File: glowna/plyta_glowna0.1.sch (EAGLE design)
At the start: 111 parts, among them IC1 4504D, Q1 CSM-7X-DU, Q2 N-HEXFET-2D_SOT232-IRLL014N, Q3 N-HEXFET-2D_SOT232-IRLL014N, Q4 N-HEXFET-2D_SOT232-IRLL014N, Q5 N-HEXFET-2D_SOT232-IRLL014N, Q6 N-HEXFET-2D_SOT232-IRLL014N, X1 MINI-USB_SHIELD5P2-32005-601

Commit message: indukcyjne
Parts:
- removed JP23: (no value), pinhead:PINHD-1X2
- added D8: BAT54S, diode:BAT54S
- added JP27: (no value), pinhead:PINHD-1X3
- C27: value 1uF -> 50nF
- R11: value 4,7k -> 5k
- R13: value 1k -> 15k
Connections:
- removed net N$16: JP23.2, R12.1
- new net N$38: JP27.1, R13.2
- net +12V: now also JP27.3; no longer R11.1
- net +3V3: now also D8.C2
- net ADC3_CZUJNIK_INDUKCYJNY: now also D8.C1A2, R11.1; no longer R11.2, R12.2
- net GND: now also D8.A1, JP27.2, R11.2; no longer R13.2
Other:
- moved on the sheet: C27, R11, R12, R13

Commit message: level shifter
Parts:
- added D_1, D_2, D_3, D_4, D_5, D_6: (no value), diode:DIODE-DO-214AC
- added R16: 300, rcl:R-EU_R0603
- R12: value 330 -> 300
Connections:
- new net N$16: IC1P.VCC, R12.1
- new net N$39: IC1P.VDD, R16.1
- net +12V: now also D_5.C, D_6.C, R16.2; no longer IC1P.VCC
- net +24V: now also D_1.C, D_2.C, D_3.C, D_4.C
- net +3V3: now also R12.2
- net GND: no longer IC1P.VDD
- net N$11: now also D_6.A
- net N$12: now also D_1.A
- net N$15: now also D_5.A
- net N$17: now also D_3.A
- net N$18: now also D_4.A
- net N$20: now also D_2.A
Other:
- moved on the sheet: IC1P, R12

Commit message: rs i termistory
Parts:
- added C28, C29, C30: 1uF, rcl:C-EUC0603
- added D1, D2, D3, D4: BAT54S, diode:BAT54S
- added IC2: MAX481CSA, maxim:MAX481CSA
- added R17: 1k, rcl:R-EU_R0603
- added R18, R19, R20, R21: 10k, rcl:R-EU_R0603
- added U$19: TS9011SCX, v-reg:TS9011SCX
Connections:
- new net N$40: C28.2, IC2P.VCC, U$19.OUT
- new net N$42: C25.2, D3.C1A2, R19.2
- new net N$43: C24.2, D2.C1A2, R20.2
- new net N$44: C26.2, D4.C1A2, R18.2
- new net N$47: C23.2, D1.C1A2, R21.2
- net +12V: now also U$19.IN
- net +3V3: now also D1.C2, D2.C2, D3.C2, D4.C2
- net ADC_TER_1: now also R20.1; no longer C24.2
- net ADC_TER_2: now also R19.1; no longer C25.2
- net ADC_TER_3: now also R18.1; no longer C26.2
- net ADC_TER_BED: now also R21.1; no longer C23.2
- net GND: now also C28.1, C29.1, C30.1, D1.A1, D2.A1, D3.A1, D4.A1, IC2P.GND, U$19.GND
- net N$16: now also C29.2
- net N$39: now also C30.2
- net RS485_UART2_RTS: now also IC2G$1.DE, IC2G$1.RE/
- net RS485_UART2_TX: now also IC2G$1.DI, IC2G$1.RO, R17.1, R17.2

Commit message: kondensatory
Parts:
- added C31: 100uF, rcl:CPOL-EUUD-8X10
- added C32: 100nF, rcl:C-EUC0603
- C20, C21, C22: value (none) -> 100uF
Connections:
- net +3V3: now also C31.+, C32.2
- net GND: now also C31.-, C32.1
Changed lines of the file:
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@@
 <part name="+3V18" library="supply1" deviceset="+3V3" device=""/>
 <part name="GND42" library="supply1" deviceset="GND" device=""/>
-<part name="C20" library="rcl" deviceset="CPOL-EU" device="UD-8X10"/>
-<part name="C21" library="rcl" deviceset="CPOL-EU" device="UD-8X10"/>
-<part name="C22" library="rcl" deviceset="CPOL-EU" device="UD-8X10"/>
+<part name="C20" library="rcl" deviceset="CPOL-EU" device="UD-8X10" value="100uF"/>
+<part name="C21" library="rcl" deviceset="CPOL-EU" device="UD-8X10" value="100uF"/>
+<part name="C22" library="rcl" deviceset="CPOL-EU" device="UD-8X10" value="100uF"/>
 <part name="GND43" library="supply1" deviceset="GND" device=""/>
 <part name="GND44" library="supply1" deviceset="GND" device=""/>
@@
 <part name="D3" library="diode" deviceset="BAT54S" device=""/>
 <part name="D4" library="diode" deviceset="BAT54S" device=""/>
+<part name="C31" library="rcl" deviceset="CPOL-EU" device="UD-8X10" value="100uF"/>
+<part name="C32" library="rcl" deviceset="C-EU" device="C0603" value="100nF"/>
 </parts>
 <sheets>
@@
 <attribute name="VALUE" x="-78.74" y="129.54" size="1.778" layer="96" rot="R180"/>
 </instance>
-<instance part="+3V16" gate="G$1" x="-114.3" y="86.36" smashed="yes" rot="R180">
-<attribute name="VALUE" x="-116.84" y="83.82" size="1.778" layer="96"/>
+<instance part="+3V16" gate="G$1" x="-114.3" y="96.52" smashed="yes">
+<attribute name="VALUE" x="-111.76" y="99.06" size="1.778" layer="96" rot="R180"/>
 </instance>
 <instance part="Q1" gate="P" x="-43.18" y="88.9" rot="R90"/>
@@
 <attribute name="VALUE" x="288.4424" y="-19.558" size="1.778" layer="96" rot="R90"/>
 </instance>
+<instance part="C31" gate="G$1" x="-119.38" y="86.36"/>
+<instance part="C32" gate="G$1" x="-109.22" y="83.82" smashed="yes" rot="R180">
+<attribute name="NAME" x="-106.299" y="89.916" size="1.778" layer="95" rot="R270"/>
+<attribute name="VALUE" x="-103.759" y="89.916" size="1.778" layer="96" rot="R270"/>
+</instance>
 </instances>
 <busses>
@@
 <pinref part="+3V15" gate="G$1" pin="+3V3"/>
 <wire x1="-81.28" y1="124.46" x2="-81.28" y2="119.38" width="0.1524" layer="91"/>
-</segment>
-<segment>
-<pinref part="U$5" gate="G$1" pin="C"/>
-<pinref part="U$6" gate="G$1" pin="OUT"/>
-<wire x1="-129.54" y1="101.6" x2="-121.92" y2="101.6" width="0.1524" layer="91"/>
-<wire x1="-121.92" y1="101.6" x2="-121.92" y2="91.44" width="0.1524" layer="91"/>
-<wire x1="-121.92" y1="91.44" x2="-114.3" y2="91.44" width="0.1524" layer="91"/>
-<junction x="-121.92" y="91.44"/>
-<pinref part="+3V16" gate="G$1" pin="+3V3"/>
-<wire x1="-114.3" y1="91.44" x2="-114.3" y2="88.9" width="0.1524" layer="91"/>
 </segment>
 <segment>
@@
 <wire x1="317.5" y1="-25.4" x2="317.5" y2="-22.86" width="0.1524" layer="91"/>
 </segment>
+<segment>
+<pinref part="U$5" gate="G$1" pin="C"/>
+<pinref part="U$6" gate="G$1" pin="OUT"/>
+<wire x1="-129.54" y1="101.6" x2="-121.92" y2="101.6" width="0.1524" layer="91"/>
+<wire x1="-121.92" y1="101.6" x2="-121.92" y2="91.44" width="0.1524" layer="91"/>
+<wire x1="-121.92" y1="91.44" x2="-119.38" y2="91.44" width="0.1524" layer="91"/>
+<junction x="-121.92" y="91.44"/>
+<pinref part="C31" gate="G$1" pin="+"/>
+<wire x1="-119.38" y1="88.9" x2="-119.38" y2="91.44" width="0.1524" layer="91"/>
+<junction x="-119.38" y="91.44"/>
+<pinref part="C32" gate="G$1" pin="2"/>
+<wire x1="-119.38" y1="91.44" x2="-114.3" y2="91.44" width="0.1524" layer="91"/>
+<wire x1="-114.3" y1="91.44" x2="-109.22" y2="91.44" width="0.1524" layer="91"/>
+<wire x1="-109.22" y1="91.44" x2="-109.22" y2="88.9" width="0.1524" layer="91"/>
+<pinref part="+3V16" gate="G$1" pin="+3V3"/>
+<wire x1="-114.3" y1="93.98" x2="-114.3" y2="91.44" width="0.1524" layer="91"/>
+<junction x="-114.3" y="91.44"/>
+</segment>
 </net>
 <net name="GND" class="0">
@@
 <pinref part="GND16" gate="1" pin="GND"/>
 <wire x1="-129.54" y1="83.82" x2="-129.54" y2="81.28" width="0.1524" layer="91"/>
-</segment>
-<segment>
+<pinref part="C31" gate="G$1" pin="-"/>
+<wire x1="-129.54" y1="81.28" x2="-119.38" y2="81.28" width="0.1524" layer="91"/>
+<junction x="-129.54" y="81.28"/>
+<pinref part="C32" gate="G$1" pin="1"/>
+<wire x1="-109.22" y1="81.28" x2="-119.38" y2="81.28" width="0.1524" layer="91"/>
+<junction x="-119.38" y="81.28"/>
+</segment>
+<segment>

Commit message: 0.1
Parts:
- added C33: 100nF, rcl:C-EUC0603
- C31: value 100uF -> 10\uF
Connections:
- net +12V: now also C33.2
- net GND: now also C33.1
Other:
- note removed: "Co robimy z rs485?"
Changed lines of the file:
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@@
 <?xml version="1.0" encoding="utf-8"?>
 <!DOCTYPE eagle SYSTEM "eagle.dtd">
-<eagle version="7.2.0">
+<eagle version="7.5.0">
 <drawing>
 <settings>
@@
 <part name="D3" library="diode" deviceset="BAT54S" device=""/>
 <part name="D4" library="diode" deviceset="BAT54S" device=""/>
-<part name="C31" library="rcl" deviceset="CPOL-EU" device="UD-8X10" value="100uF"/>
+<part name="C31" library="rcl" deviceset="CPOL-EU" device="UD-8X10" value="10\uF"/>
 <part name="C32" library="rcl" deviceset="C-EU" device="C0603" value="100nF"/>
+<part name="C33" library="rcl" deviceset="C-EU" device="C0603" value="100nF"/>
 </parts>
 <sheets>
@@
 <text x="-45.72" y="71.12" size="1.27" layer="99">Wyliczymy jak
 już będzie dobrany kwarc</text>
-<text x="88.9" y="121.92" size="2.54" layer="99">Co robimy z rs485?</text>
 <wire x1="-48.26" y1="134.62" x2="-104.14" y2="134.62" width="0.1524" layer="97" style="longdash"/>
 <wire x1="-104.14" y1="134.62" x2="-104.14" y2="60.96" width="0.1524" layer="97" style="longdash"/>
@@
 <instance part="U$4" gate="G$1" x="-63.5" y="101.6"/>
 <instance part="U$5" gate="G$1" x="-129.54" y="106.68"/>
-<instance part="U$6" gate="G$1" x="-129.54" y="91.44"/>
+<instance part="U$6" gate="G$1" x="-129.54" y="91.44" smashed="yes">
+<attribute name="NAME" x="-139.7" y="83.82" size="1.778" layer="95"/>
+<attribute name="VALUE" x="-139.7" y="81.28" size="1.778" layer="96"/>
+</instance>
 <instance part="R3" gate="G$1" x="-139.7" y="99.06" smashed="yes" rot="R270">
 <attribute name="NAME" x="-146.05" y="100.5586" size="1.778" layer="95"/>
@@
 <attribute name="VALUE" x="-103.759" y="89.916" size="1.778" layer="96" rot="R270"/>
 </instance>
+<instance part="C33" gate="G$1" x="157.48" y="10.16" rot="R180"/>
 </instances>
 <busses>
@@
 <wire x1="182.88" y1="2.54" x2="182.88" y2="10.16" width="0.1524" layer="91"/>
 <junction x="177.8" y="2.54"/>
+<pinref part="C33" gate="G$1" pin="1"/>
+<wire x1="167.64" y1="2.54" x2="157.48" y2="2.54" width="0.1524" layer="91"/>
+<wire x1="157.48" y1="2.54" x2="157.48" y2="7.62" width="0.1524" layer="91"/>
 </segment>
 </net>
@@
 <pinref part="U$19" gate="G$1" pin="IN"/>
 <pinref part="P+24" gate="1" pin="+12V"/>
-<wire x1="160.02" y1="22.86" x2="154.94" y2="22.86" width="0.1524" layer="91"/>
+<wire x1="160.02" y1="22.86" x2="157.48" y2="22.86" width="0.1524" layer="91"/>
+<wire x1="157.48" y1="22.86" x2="154.94" y2="22.86" width="0.1524" layer="91"/>
 <wire x1="154.94" y1="22.86" x2="154.94" y2="25.4" width="0.1524" layer="91"/>
+<pinref part="C33" gate="G$1" pin="2"/>
+<wire x1="157.48" y1="15.24" x2="157.48" y2="22.86" width="0.1524" layer="91"/>
+<junction x="157.48" y="22.86"/>
 </segment>
 </net>

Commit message: zabezpieczenia
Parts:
- added D10, D11, D12, D13, D14, D15, D16, D17, D18, D19, D20, D5, D6, D7, D9: BAT54S, diode:BAT54S
- added R22, R23, R24, R25, R26, R27, R28, R29, R30, R31, R32, R33, R34, R35, R36: 1k, rcl:R-EU_R0603
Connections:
- new net N$41: D5.C1A2, JP1.4, R22.2
- new net N$45: D6.C1A2, JP1.3, R23.2
- new net N$46: D7.C1A2, JP1.2, R24.2
- new net N$48: D16.C1A2, JP4.4, R31.2
- new net N$49: D9.C1A2, JP2.4, R25.2
- new net N$50: D10.C1A2, JP2.3, R26.2
- new net N$51: D15.C1A2, JP4.3, R32.2
- new net N$52: D12.C1A2, JP3.4, R28.2
- new net N$53: D13.C1A2, JP3.3, R29.2
- new net N$54: R30.1
- new net N$55: D18.C1A2, JP5.4, R33.2
- new net N$56: D17.C1A2, JP5.3, R34.2
- new net N$57: D11.C1A2, JP2.2, R27.2
- new net N$58: D20.C1A2, JP6.4, R35.2
- new net N$59: D19.C1A2, JP6.3, R36.2
- net +3V3: now also D10.C2, D11.C2, D12.C2, D13.C2, D14.C2, D15.C2, D16.C2, D17.C2, D18.C2, D19.C2, D20.C2, D5.C2, D6.C2, D7.C2, D9.C2
- net GND: now also D10.A1, D11.A1, D12.A1, D13.A1, D14.A1, D15.A1, D16.A1, D17.A1, D18.A1, D19.A1, D20.A1, D5.A1, D6.A1, D7.A1, D9.A1
- net TIM12_EX2_1: now also R34.1; no longer JP5.3
- net TIM12_EX2_2: now also R33.1; no longer JP5.4
- net TIM4_PWM_X1: now also R24.1; no longer JP1.2
- net TIM4_PWM_X2: now also R23.1; no longer JP1.3
- net TIM4_PWM_X3: now also R22.1; no longer JP1.4
- net TIM5_EX1_1: now also R32.1; no longer JP4.3
- net TIM5_PWM_Y1: now also R27.1; no longer JP2.2
- net TIM5_PWM_Y2: now also R26.1; no longer JP2.3
- net TIM5_PWM_Y3: now also R25.1; no longer JP2.4
- net TIM8_EX1_2: now also R31.1; no longer JP4.4
- net TIM8_PWM_Z1: now also D14.C1A2, R30.2
- net TIM8_PWM_Z2: now also R29.1; no longer JP3.3
- net TIM8_PWM_Z3: now also R28.1; no longer JP3.4
- net TIM9_EX3_1: now also R36.1; no longer JP6.3
- net TIM9_EX3_2: now also R35.1; no longer JP6.4
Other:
- moved on the sheet: JP4, JP5, JP6

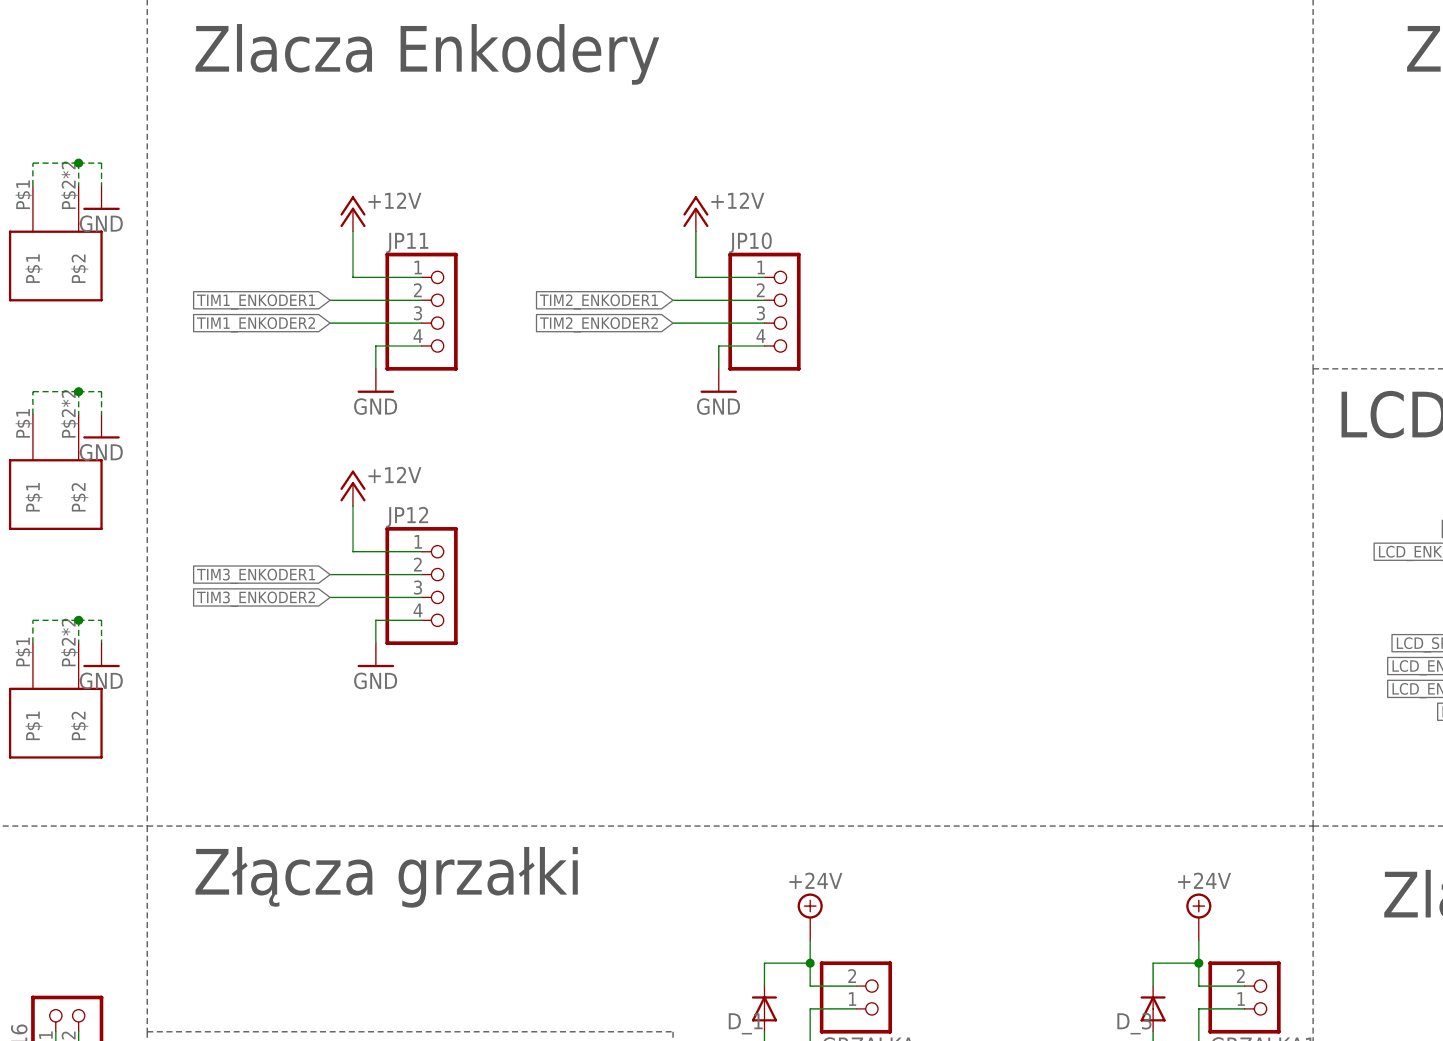
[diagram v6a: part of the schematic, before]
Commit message: zabezpieczenie i filtr do enkoderow
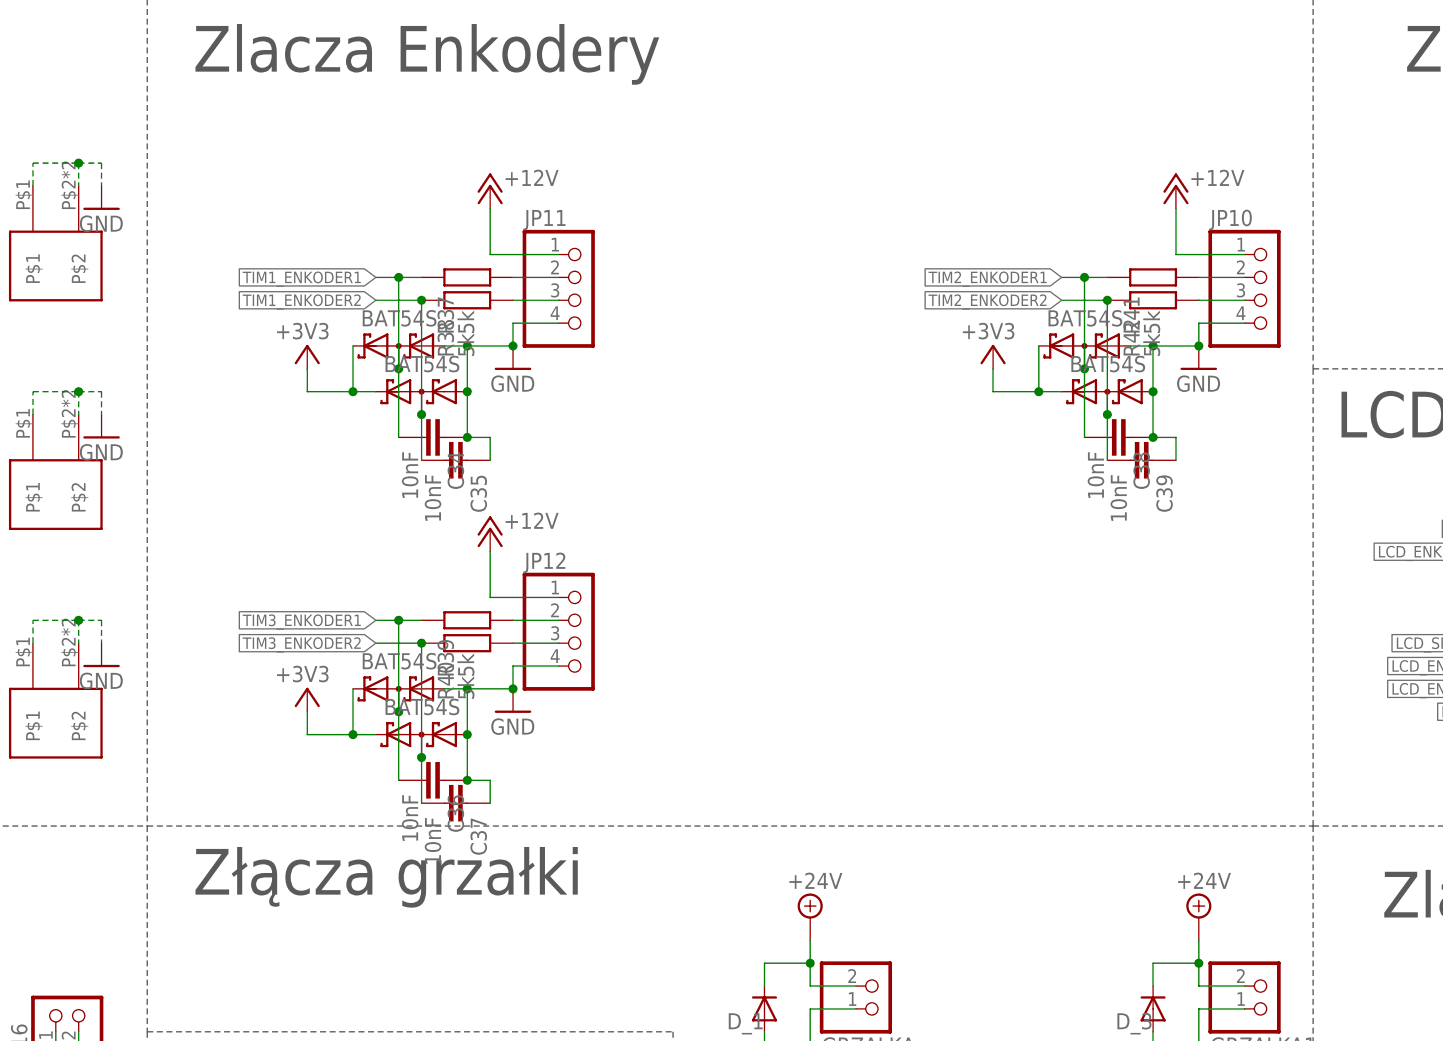
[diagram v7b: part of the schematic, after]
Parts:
- added C34, C35, C36, C37, C38, C39: 10nF, rcl:C-EUC0603
- added D21, D22, D23, D24, D25, D26: BAT54S, diode:BAT54S
- added R37, R38, R39, R40, R41, R42: 5k, rcl:R-EU_R0603
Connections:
- new net N$60: JP11.2, R37.2
- new net N$61: JP11.3, R38.2
- new net N$62: JP12.2, R39.2
- new net N$63: JP12.3, R40.2
- new net N$64: JP10.2, R41.2
- new net N$65: JP10.3, R42.2
- net +3V3: now also D21.C2, D22.C2, D23.C2, D24.C2, D25.C2, D26.C2
- net GND: now also C34.1, C35.1, C36.1, C37.1, C38.1, C39.1, D21.A1, D22.A1, D23.A1, D24.A1, D25.A1, D26.A1
- net TIM1_ENKODER1: now also C34.2, D21.C1A2, R37.1; no longer JP11.2
- net TIM1_ENKODER2: now also C35.2, D22.C1A2, R38.1; no longer JP11.3
- net TIM2_ENKODER1: now also C38.2, D25.C1A2, R41.1; no longer JP10.2
- net TIM2_ENKODER2: now also C39.2, D26.C1A2, R42.1; no longer JP10.3
- net TIM3_ENKODER1: now also C36.2, D23.C1A2, R39.1; no longer JP12.2
- net TIM3_ENKODER2: now also C37.2, D24.C1A2, R40.1; no longer JP12.3
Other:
- note added: "<-- To coś chcę wyłączać"
- moved on the sheet: JP10, JP11, JP12

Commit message: silniki - sterowanie
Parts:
- added IC3: 4504D, 45xx:4504D
- added R43, R44, R45, R46, R47, R48: 440, rcl:R-EU_R0603
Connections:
- net TIM8_EX1_2 renamed TIM8_EX3_2
- net TIM9_EX3_1 renamed TIM9_EX1_1
- net TIM9_EX3_2 renamed TIM9_EX1_2
- new net MLOG_1: JP1.1, R43.2
- new net MLOG_2: JP2.1, R44.2
- new net MLOG_3: JP3.1, R45.2
- new net MLOG_4: JP6.1, R46.2
- new net MLOG_5: JP5.1, R47.2
- new net MLOG_6: JP4.1, R48.2
- new net M_EN1: IC3A.AI
- new net M_EN3: U$1.PE2
- new net N$67: IC3A.AO, R43.1
- new net N$68: IC3A.BO, R44.1
- new net N$69: IC3A.CO, R45.1
- new net N$70: IC3A.DO, R46.1
- new net N$71: IC3A.EO, R47.1
- new net N$72: IC3A.FO, R48.1
- new net TIM5_EX3_1: R32.1
- net +12V: now also IC3P.VDD; no longer JP1.1, JP2.1, JP3.1, JP4.1, JP5.1, JP6.1
- net +3V3: now also IC3P.VCC
- net GND: now also IC3A.MODE, IC3P.GND
- net TIM5_EX1_1: no longer R32.1
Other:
- note removed: "Co lubisz? sieka? to może coś w stylu Gundam 00"
- note removed: "Jest miejsce to napisz anime jakieś fajne bo tamto już kończę"
- note removed: "Offtopic"
- moved on the sheet: JP4, JP6, R31, R32, R35, R36
